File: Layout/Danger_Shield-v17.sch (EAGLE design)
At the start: 35 parts, among them U1 ARDUINO_SHIELDNO_SILK, U2 74LS595N, U3 LM335

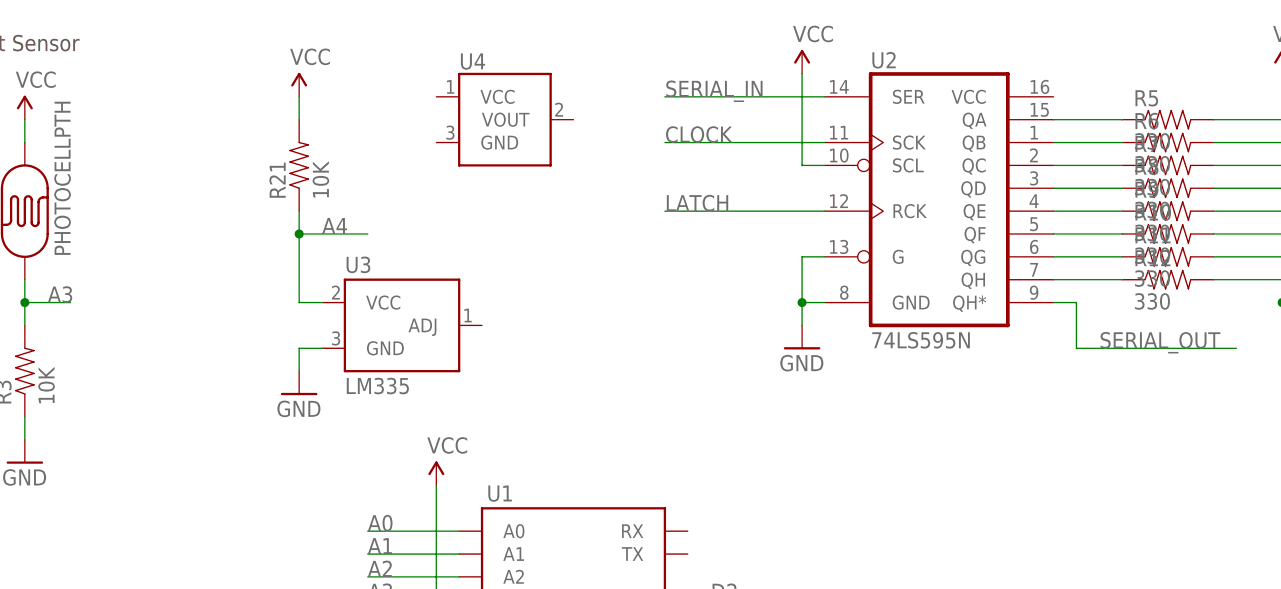
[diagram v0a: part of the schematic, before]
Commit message: v1.7 changes temp sensor to TMP36. Add 2 caps.
Removed 10k on temp sensor. Changed to TMP36. Added 2 x 0.1uF caps for
decoupling on shift register and temp sensor.
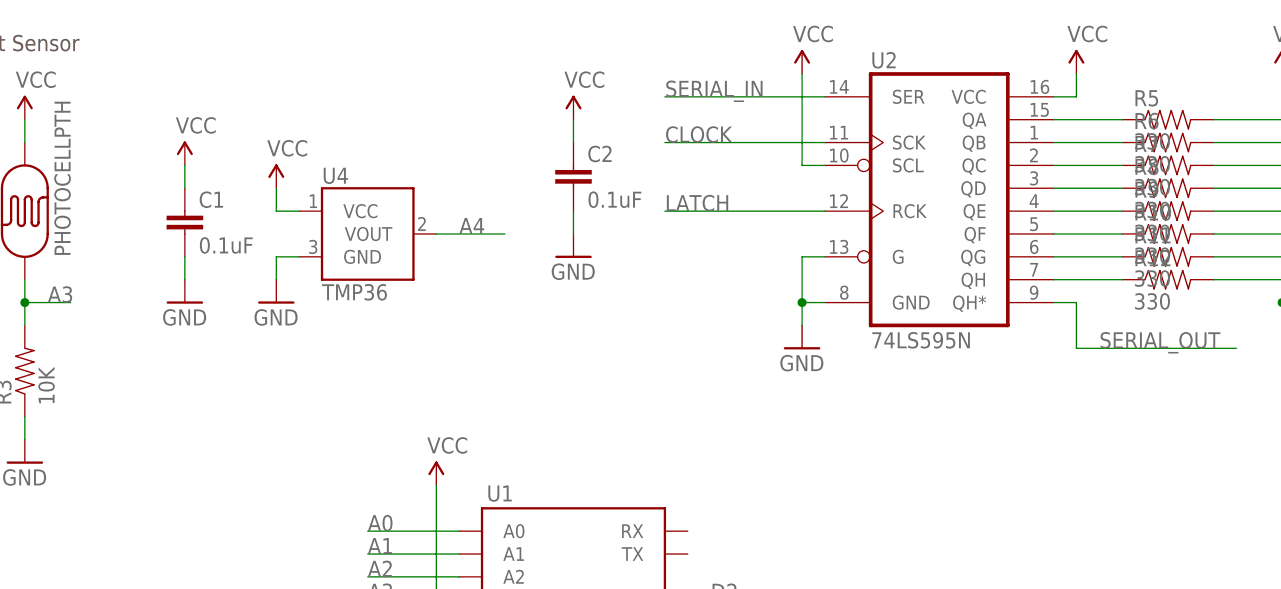
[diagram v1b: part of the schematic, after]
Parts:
- removed R21: 10K, SparkFun:RESISTORAXIAL-0.3
- removed U3: LM335, SparkFun:TEMPERATURE-SENSOR
- added C1, C2: 0.1uF, SparkFun-Passives:CAPPTH2
- U4: value (none) -> TMP36
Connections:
- net A4: now also U4.VOUT; no longer R21.1, U3.VCC
- net GND: now also C1.2, C2.2, U4.GND; no longer U3.GND
- net VCC: now also C1.1, C2.1, U2.VCC, U4.VCC; no longer R21.2
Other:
- moved on the sheet: U4
